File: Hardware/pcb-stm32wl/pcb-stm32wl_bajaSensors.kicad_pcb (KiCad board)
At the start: 4 copper layers, 33.5 x 61 mm, 182 parts, among them J1 S1001-46R, J10 Qwiic, J2 JST-PH, J3 S1001-46R, J4 RF_Shield_One_Piece, J5 S1001-46R, J6 S1001-46R, J7 U.FL/iPEX, J8 DEBUG, J9 UART/I2C, Q1 PMV32UP,215, Q2 PMST4401,115, SW1 USR_BTN, SW2 RESET, U1 TPS22917DBV, U10 SHTC3, U11 ATECC608B-TNGLORAU, U2 TPS3839G18DBZT‎, U3 TPS22917DBV, U4 RP605Z283B, U5 STM32WL55CCU6, U6 TS3A5223RSWR, U7 BGS13S4N9, U8 MX25R1635, U9 LIS2DH12, X1 32MHz, Y1 32.768KHz

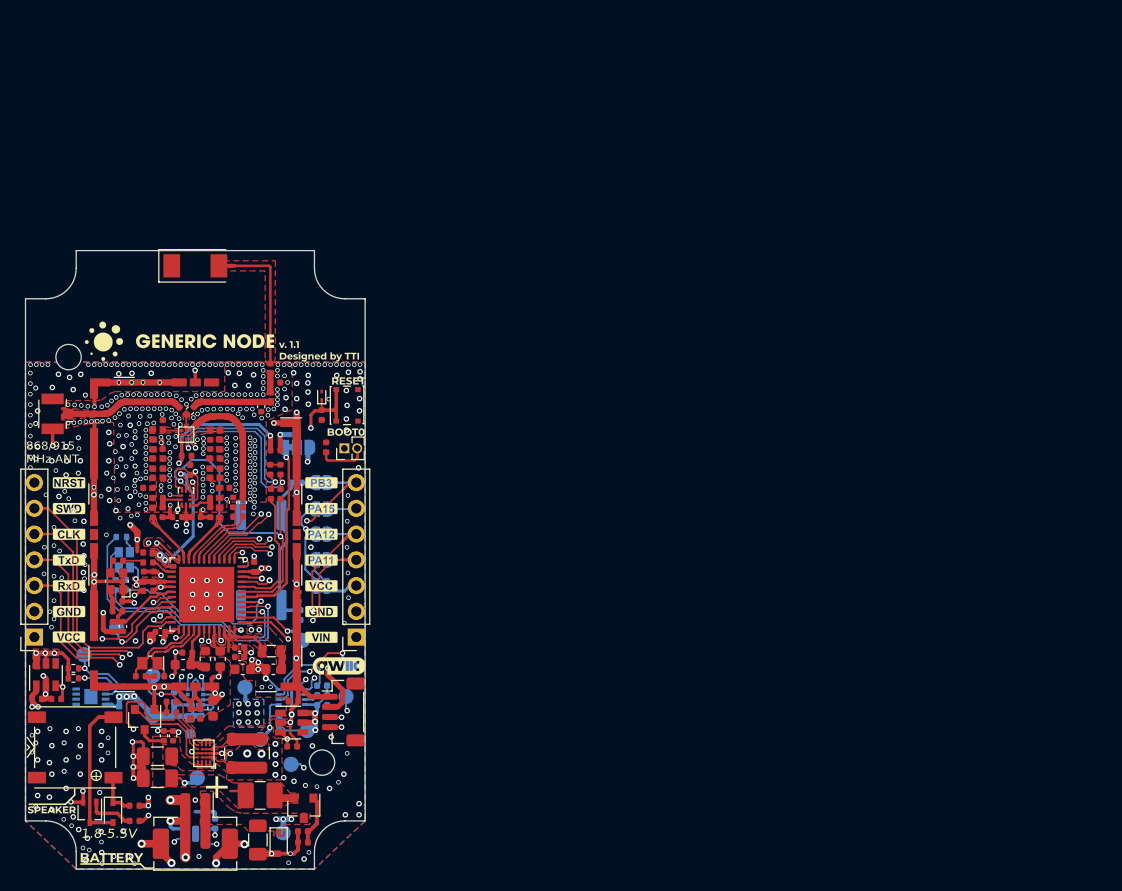
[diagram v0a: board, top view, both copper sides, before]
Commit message: rewried circuit to account ofr small details
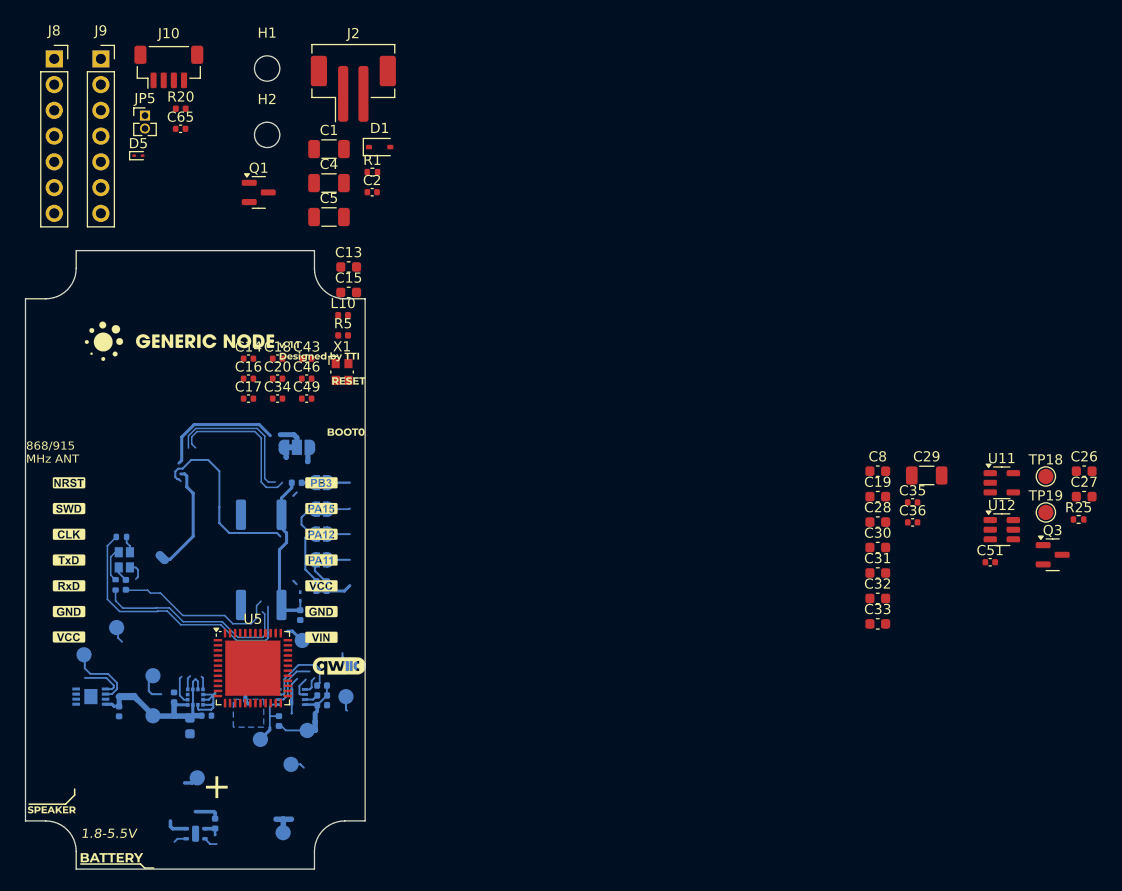
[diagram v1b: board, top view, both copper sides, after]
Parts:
- removed AE1: NN02-201, node-lib-v1:Antenna_Fractus_NN02-201
- removed C10, C24, C57, C7, C9: 100nF, Capacitor_SMD:C_0402_1005Metric
- removed C11, C3, C6: 1uF, Capacitor_SMD:C_0402_1005Metric
- removed C12: 22uF, Capacitor_SMD:C_0603_1608Metric
- removed C21, C22, C41, C42: 33pF, Capacitor_SMD:C_0402_1005Metric
- removed C23: 47pF, Capacitor_SMD:C_0402_1005Metric
- removed C25: 47nF, Capacitor_SMD:C_0402_1005Metric
- removed C37, C44: 2.7pF, Capacitor_SMD:C_0402_1005Metric
- removed C38: 2.4pF, Capacitor_SMD:C_0402_1005Metric
- removed C39: 3.3pF, Capacitor_SMD:C_0402_1005Metric
- removed C40: 3.9pF, Capacitor_SMD:C_0402_1005Metric
- removed C45: 1.3pF, Capacitor_SMD:C_0402_1005Metric
- removed C47, C48, C50: 1nF, Capacitor_SMD:C_0402_1005Metric
- removed C55: DNM, Capacitor_SMD:C_0402_1005Metric
- removed D2: 1N4148WSF-7, node-lib-v1:D_SOD-323F_custom
- removed F1: PTC 13V 1A, Fuse:Fuse_1210_3225Metric_Castellated
- removed FB1: 600R @100MHz, Inductor_SMD:L_0603_1608Metric
- removed J1, J3, J5, J6: S1001-46R, node-lib-v1:RF_Shield_Clip_S1001-46R
- removed J4: RF_Shield_One_Piece, node-lib-v1:RF_Shield_SnapOn_30x20mm_w_Cutout_n_GND_Pads
- removed J7: U.FL/iPEX, Connector_Coaxial:U.FL_Hirose_U.FL-R-SMT-1_Vertical
- removed L1: 2.2uH, node-lib-v1:L_HPC4012TF-2R2M
- removed L11: 6.8nH, Inductor_SMD:L_0402_1005Metric
- removed L12: 8.7nH, Inductor_SMD:L_0402_1005Metric
- removed L13: 27nH, Inductor_SMD:L_0402_1005Metric
- removed L14: 6.5nH, Inductor_SMD:L_0402_1005Metric
- removed L15: 8nH, Inductor_SMD:L_0402_1005Metric
- removed L2, L9: 3.3nH, Inductor_SMD:L_0402_1005Metric
- removed L3: 3.6nH, Inductor_SMD:L_0402_1005Metric
- removed L4: 15uH, node-lib-v1:L_0805_2012Metric_custom
- removed L5: 11nH, Inductor_SMD:L_0402_1005Metric
- removed L6, L7: 47nH, Inductor_SMD:L_0402_1005Metric
- removed L8: 3nH, Inductor_SMD:L_0402_1005Metric
- removed PZ1: MLT-7525, node-lib-v1:Buzzer_MLT-7525
- removed Q2: PMST4401,115, Package_TO_SOT_SMD:SOT-323_SC-70
- removed R10: DNM, Resistor_SMD:R_0402_1005Metric
- removed R14, R17: 4K7, Resistor_SMD:R_0402_1005Metric
- removed R16: 1K, Resistor_SMD:R_0402_1005Metric
- removed R19: 33R, Resistor_SMD:R_0402_1005Metric
- removed R2, R3, R4: 100K, Resistor_SMD:R_0402_1005Metric
- removed R6, R7, R8: 100R, Resistor_SMD:R_0402_1005Metric
- removed R9: 0R, Resistor_SMD:R_0402_1005Metric
- removed SW2: RESET, node-lib-v1:SW_SPST_SKSHABE010
- removed U1, U3: TPS22917DBV, Package_TO_SOT_SMD:SOT-23-6
- removed U2: TPS3839G18DBZT‎, Package_TO_SOT_SMD:SOT-23
- removed U4: RP605Z283B, node-lib-v1:WLCSP-20-P3_1.994x1.609mm_Layout5x4_P0.4mm
- removed U6: TS3A5223RSWR, Package_DFN_QFN:UQFN-10_1.4x1.8mm_P0.4mm
- removed U7: BGS13S4N9, node-lib-v1:RFSW_BGS13S4N9E6327XTSA1
- removed Y1: 32.768KHz, node-lib-v1:Crystal_SMD_NX2012SA_32.768KHz
- added C51: 1uF, Capacitor_SMD:C_0402_1005Metric, F.Cu at (228.4, 105.2)
- added Q3: PMV32UP,215, Package_TO_SOT_SMD:SOT-23, F.Cu at (234.6, 104.5)
- added R25: 100K, Resistor_SMD:R_0402_1005Metric, F.Cu at (237.1, 101.0)
- added TP18: VBAT_READ_EN, TestPoint:TestPoint_Pad_D1.5mm, F.Cu at (233.9, 96.8)
- added TP19: VBAT_ADC, TestPoint:TestPoint_Pad_D1.5mm, F.Cu at (233.9, 100.3)
- added U11: MIC5365-3.3YD5, Package_TO_SOT_SMD:SOT-23-5, F.Cu at (229.5, 97.4)
- added U12: TPS22917DBV, Package_TO_SOT_SMD:SOT-23-6, F.Cu at (229.5, 102.0)
- C19, C32, C33: value 33pF -> 0.1uF; footprint Capacitor_SMD:C_0402_1005Metric -> Capacitor_SMD:C_0603_1608Metric
- C26: value 68pF -> 4.7uF; footprint Capacitor_SMD:C_0402_1005Metric -> Capacitor_SMD:C_0603_1608Metric
- C28: value 470nF -> 0.1uF
- C29: value 100nF -> 10uF; footprint Capacitor_SMD:C_0402_1005Metric -> Capacitor_SMD:C_1206_3216Metric
- C30: value 2.7pF -> 0.1uF; footprint Capacitor_SMD:C_0402_1005Metric -> Capacitor_SMD:C_0603_1608Metric
- C31: value 3.6pF -> 0.1uF; footprint Capacitor_SMD:C_0402_1005Metric -> Capacitor_SMD:C_0603_1608Metric
- C35: value 5.6pF -> 1uF
- C36: value 6.8pF -> 1uF
- C8: value 1uF -> 0.1uF; footprint Capacitor_SMD:C_0402_1005Metric -> Capacitor_SMD:C_0603_1608Metric
- moved C26 89.6 mm to (237.7, 96.3), turned to 0 degrees
- moved C27 84.7 mm to (237.7, 98.8)
- moved C36 75.5 mm to (220.8, 101.3)
- moved J2 74.4 mm to (165.6, 58.5), turned to 0 degrees
- moved C19 71.9 mm to (217.3, 98.8), turned to 0 degrees
- moved C32 71.0 mm to (217.3, 108.8), turned to 0 degrees
- moved C29 69.9 mm to (222.1, 96.7)
- moved D1 69.4 mm to (168.2, 64.3), turned to 0 degrees
- moved H1 68.7 mm to (157.1, 56.5)
- moved C1 68.5 mm to (163.2, 64.5), turned to 0 degrees
- moved C35 67.9 mm to (220.8, 99.3), turned to 0 degrees
- moved C33 66.8 mm to (217.3, 111.3), turned to 0 degrees
- moved J10 65.9 mm to (147.4, 56.4), turned to 0 degrees
- moved R1 65.4 mm to (167.5, 66.8)
- moved C2 64.5 mm to (167.4, 68.7), turned to 0 degrees
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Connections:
- C13 pad 1: VDDRF -> +3.3V
- C14 pad 1: VDDRF -> +3.3V
- C15 pad 1: VDDA -> +3.3V
- C16 pad 1: VDDRF -> +3.3V
- C17 pad 1: VDDA -> +3.3V
- C18 pad 1: VDDRF -> +3.3V
- C19 pad 1: VDDRF -> Net-(U3-REGCAPA)
- C20 pad 1: VDDRF -> +3.3V
- C26 pad 1: Net-(C25-Pad2) -> 5V
- C27 pad 1: VDDRF -> +3.3V
- C28 pad 1: VDDRF1V55 -> +3.3V
- C29 pad 1: VDDRF -> +3.3V
- C30 pad 1: GND -> +3.3V
- C30 pad 2: /LoRa MCU/RFI_N -> GND
- C31 pad 1: /LoRa MCU/RFI_P -> +3.3V
- C31 pad 2: Net-(C31-Pad2) -> GND
- C32 pad 1: GND -> +3.3V
- C32 pad 2: Net-(C32-Pad2) -> GND
- C33 pad 1: Net-(C33-Pad1) -> +3.3V
- C35 pad 1: GND -> +3.3V
- C35 pad 2: Net-(C35-Pad2) -> GND
- C36 pad 1: GND -> +3.3V
- C36 pad 2: Net-(C36-Pad2) -> GND
- C8 pad 1: VDDRF -> Net-(U3-REGCAPD)
- D3 pad 3: VDDRF -> +3.3V
- J10 pad 2: VDDRF -> +3.3V
- J8 pad 1: VDDRF -> +3.3V
- J9 pad 3: VDDRF -> +3.3V
- J9 pad 6: /LoRa MCU/PA15 -> unconnected-(J9-Pin_6-Pad6)
- JP5 pad 1: VDDRF -> +3.3V
- TP7 pad 1: /Peripherals/MISO -> /LoRa MCU/PA6_MISO1
- TP9 pad 1: /Peripherals/MOSI -> /LoRa MCU/PA7_MOSI1
- U5 pad 11: VDDRF -> +3.3V
- U5 pad 12: /Peripherals/FlashCS -> /LoRa MCU/PA4_CS1
- U5 pad 14: /Peripherals/MISO -> /LoRa MCU/PA6_MISO1
- U5 pad 15: /Peripherals/MOSI -> /LoRa MCU/PA7_MOSI1
- U5 pad 20: /LoRa MCU/RFI_P -> unconnected-(U5-RFI_P-Pad20)
- U5 pad 21: /LoRa MCU/RFI_N -> unconnected-(U5-RFI_N-Pad21)
- U5 pad 22: Net-(L2-Pad1) -> unconnected-(U5-RFO_LP-Pad22)
- U5 pad 23: Net-(L3-Pad1) -> unconnected-(U5-RFO_HP-Pad23)
- U5 pad 24: Net-(C25-Pad2) -> unconnected-(U5-VR_PA-Pad24)
- U5 pad 25: VDDPA -> unconnected-(U5-VDDPA-Pad25)
- U5 pad 26: OSC_IN -> /LoRa MCU/HS_OUT
- U5 pad 27: (no net) -> /LoRa MCU/HS_IN
- U5 pad 28: VDDRF -> unconnected-(U5-VDDRF-Pad28)
- U5 pad 29: VDDRF1V55 -> unconnected-(U5-VDDRF1V55-Pad29)
- U5 pad 30: PB0_VDD_TCXO -> unconnected-(U5-PB0-VDD_TCXO-Pad30)
- U5 pad 32: /Power Supply/LS1_SENSORS_EN -> /LoRa MCU/PB12
- U5 pad 37: VDDRF -> +3.3V
- U5 pad 38: /Power Supply/LS2_FLASH_EN -> /LoRa MCU/PC13
- U5 pad 41: VDDA -> +3.3V
- U5 pad 44: VDDRF -> +3.3V
- U5 pad 45: VDDRF1V55 -> unconnected-(U5-VFBSMPS-Pad45)
- U5 pad 46: VDDRF -> unconnected-(U5-VDDSMPS-Pad46)
- U5 pad 47: VLXSMPS -> unconnected-(U5-VLXSMPS-Pad47)
- U5 pad 48: GND -> unconnected-(U5-VSSSMPS-Pad48)
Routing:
- net GND: track 198.1 -> 18.5 mm, vias 496 -> 0
- net (no net): track 8.19 -> 85.4 mm, vias 6 -> 0
- net /LoRa MCU/PA09_SCL1: track 72.8 -> 9.87 mm, vias 5 -> 0
- net /LoRa MCU/NRST: track 56.6 -> 0.00 mm, vias 2 -> 0
- net VDDRF: track 166.3 -> 119.2 mm, vias 22 -> 0
- net /Peripherals/VCC_SENSORS: track 66.8 -> 23.1 mm, vias 7 -> 0
- net /LoRa MCU/PA2_TxD2: track 42.1 -> 0.00 mm, vias 2 -> 0
- net /LoRa MCU/PA10_SDA1: track 51.2 -> 9.25 mm, vias 4 -> 0
- net /LoRa MCU/PA3_RxD2: track 41.7 -> 0.00 mm, vias 2 -> 0
- net /LoRa MCU/PB4: track 63.3 -> 28.1 mm, vias 3 -> 0
- net /Peripherals/MOSI: track 36.7 -> 1.80 mm, vias 3 -> 0
- net /Power Supply/LS2_FLASH_EN: track 34.7 -> 0.00 mm, vias 2 -> 0
- net /LoRa MCU/PA12_SCL2: track 57.3 -> 23.3 mm, vias 3 -> 0
- net VDDRF1V55: track 33.6 -> 0.00 mm, vias 6 -> 0
- net /LoRa MCU/BOOT0: track 30.4 -> 0.00 mm, vias 1 -> 0
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- added copper zone on B.Cu, net +3.3V
- added copper zone on In2.Cu, net +3.3V
- removed copper zone on F.Cu, net +BATT
- removed copper zone on F.Cu, net /Peripherals/VCC_SENSORS
- removed copper zone on B.Cu, net GND
- removed copper zone on F.Cu, net GND
- removed copper zone on In1.Cu, net GND
- removed copper zone on In2.Cu, net GND
- removed copper zone on F.Cu, net Net-(AE1-Pad2)
- removed copper zone on F.Cu, net Net-(C25-Pad2)
- removed copper zone on F.Cu, net Net-(C31-Pad2)
- removed copper zone on F.Cu, net Net-(C35-Pad2)
- removed copper zone on F.Cu, net Net-(C36-Pad2)
- removed copper zone on F.Cu, net Net-(C37-Pad2)
- removed copper zone on F.Cu, net Net-(C38-Pad2)
- removed copper zone on F.Cu, net Net-(C41-Pad2)
- removed copper zone on F.Cu, net Net-(C42-Pad2)
- removed copper zone on F.Cu, net Net-(C44-Pad2)
- removed copper zone on F.Cu, net Net-(C45-Pad2)
- removed copper zone on F.Cu, net Net-(C54-Pad1)
- removed copper zone on F.Cu, net Net-(C54-Pad2)
- removed copper zone on F.Cu, net Net-(J7-Pad1)
- removed copper zone on F.Cu, net Net-(L1-Pad1)
- removed copper zone on F.Cu, net Net-(L1-Pad2)
- removed copper zone on F.Cu, net Net-(L13-Pad1)
- removed copper zone on F.Cu, net Net-(L2-Pad1)
- removed copper zone on F.Cu, net Net-(L3-Pad1)
- removed copper zone on F.Cu, net Net-(Q1-S)
- removed copper zone on F.Cu, net Net-(R10-Pad2)
- removed copper zone on F.Cu, net VDDPA
- removed copper zone on B.Cu, net VDDRF
- removed copper zone on F.Cu, net VDDRF
- removed copper zone on In2.Cu, net VDDRF
- removed copper zone on F.Cu, net VDDRF1V55
- removed copper zone on F.Cu, net VLXSMPS
- removed copper zone on F.Cu, net Vin
